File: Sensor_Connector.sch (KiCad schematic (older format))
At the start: 7 parts, among them J3 JST-GH

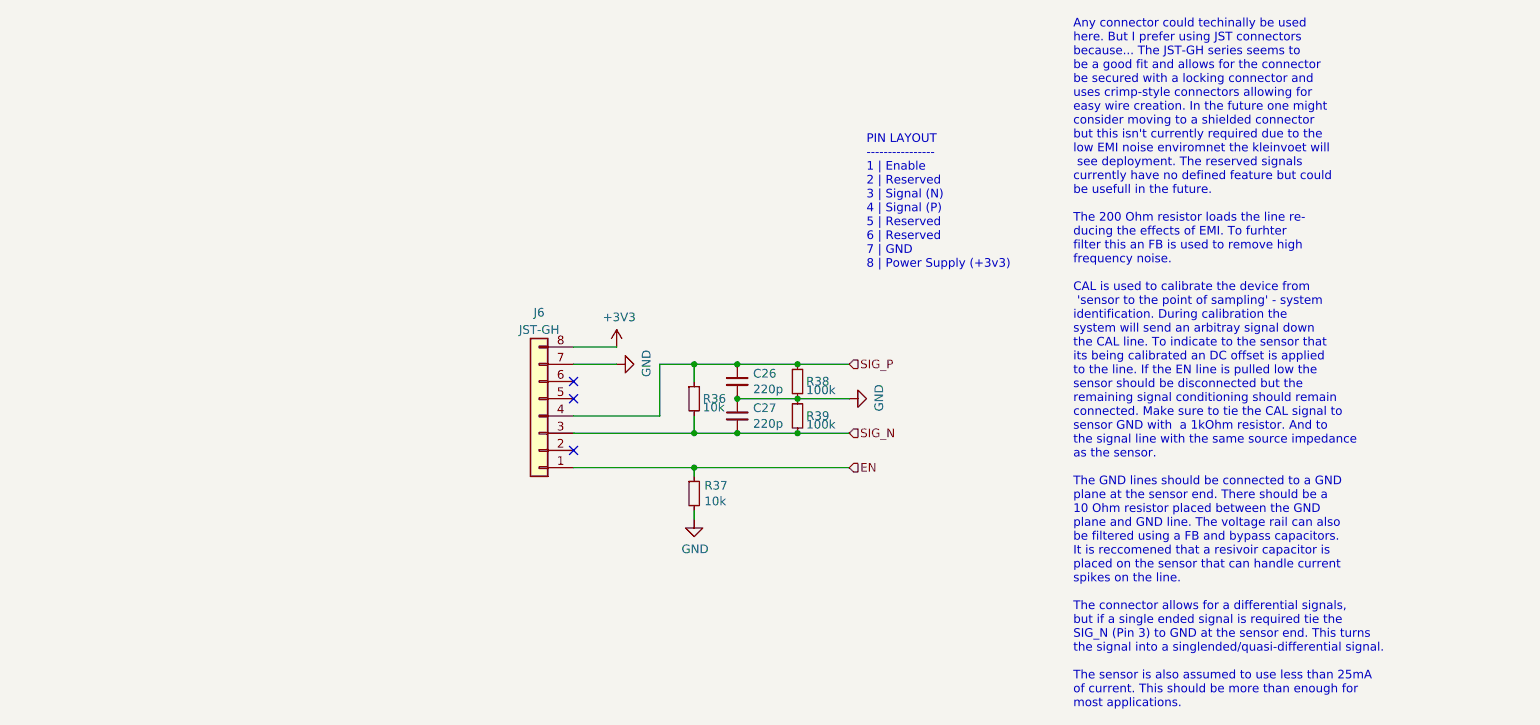
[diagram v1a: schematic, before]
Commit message: Change Mic Preamp
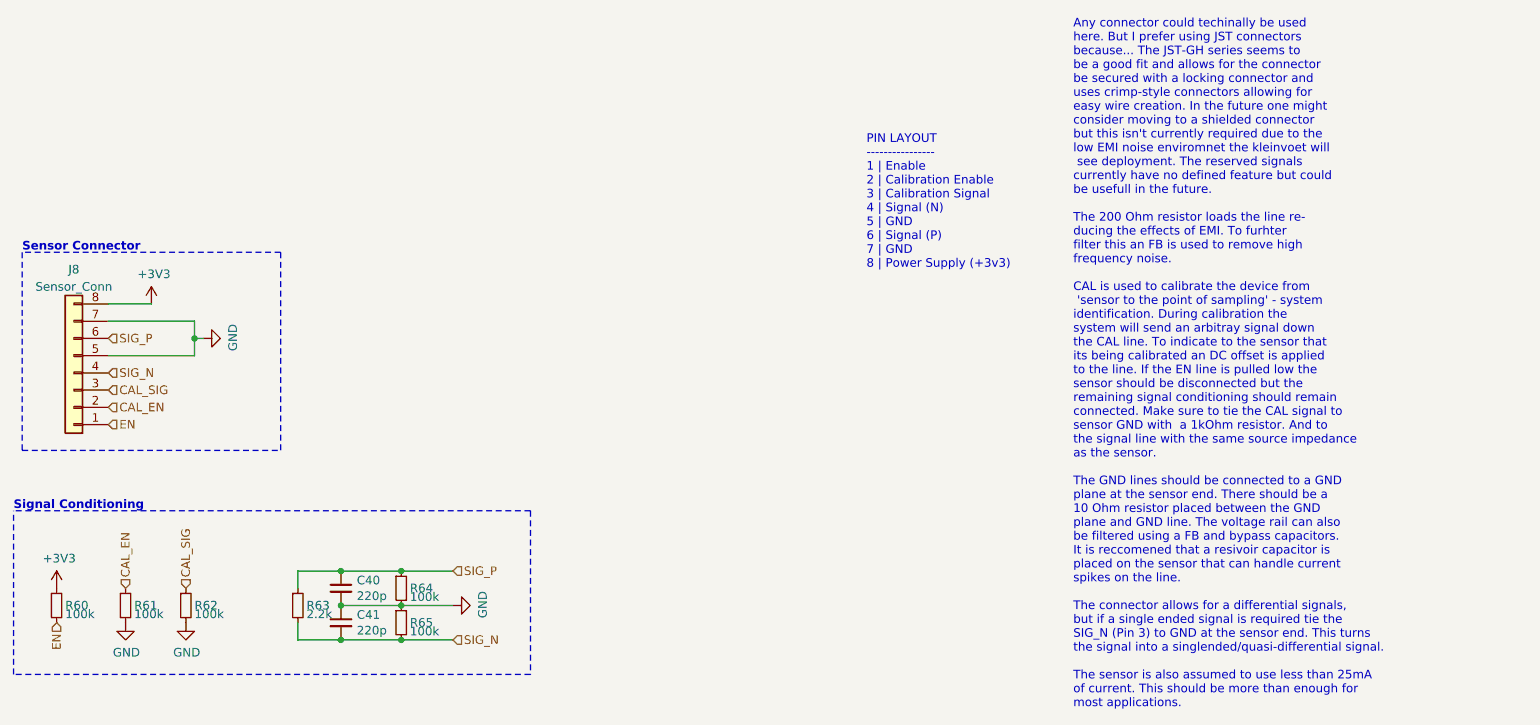
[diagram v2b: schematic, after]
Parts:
- added R24, R26: 100k, Resistor_SMD:R_0603_1608Metric_Pad1.05x0.95mm_HandSolder, symbol Device:R_Small
- J3: value JST-GH -> Sensor_Conn
- R25: value 10k -> 100k; MPN (none) -> RC0603FR-07100KL; Mfr. (none) -> Yageo
- R27: renamed from R24; value 10k -> 2.2k; MPN RC0603JR-0710KL -> RC0603FR-072K2L
- renumbered C20 to C18, C21 to C19, R26 to R28, R27 to R29
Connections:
- net +3V3: now also R24.1
- net EN: now also R24.2; no longer R25.1
- net GND: now also J3.5 (Pin_5), R26.2
- net SIG_N: now also J3.4 (Pin_4); no longer J3.3 (Pin_3)
- net SIG_P: now also J3.6 (Pin_6); no longer J3.4 (Pin_4)
- net CAL_EN: now reaches J3.2 (Pin_2)
- net CAL_EN: now also R25.1
- new net CAL_SIG: J3.3 (Pin_3), R26.1
- no-connect marks 3 -> 0
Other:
- note added: "PIN LAYOUT\n----------------\n1 | Enable\n2 | Calibration Enable\n3 | Calibration Signal\n4 | Signal (N)\n5 | GND\n6 | Signal (P)\n7 | GND\n8 | Power Supply (+3v3)"
- note added: "Sensor Connector"
- note added: "Signal Conditioning"
- note removed: "PIN LAYOUT\n----------------\n1 | Enable\n2 | Reserved\n3 | Signal (N)\n4 | Signal (P)\n5 | Reserved\n6 | Reserved\n7 | GND\n8 | Power Supply (+3v3)"
- moved on the sheet: C40, C41, J8, R63, R64, R65

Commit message: Fix BOM ref
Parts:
- C18, C19: MPN (none) -> C0603C221J5GACTU; Mfr. (none) -> KEMET
- J3: MPN (none) -> 53047-0810; Mfr. (none) -> Molex
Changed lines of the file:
@@
 $Descr A4 11693 8268
 encoding utf-8
-Sheet 12 15
+Sheet 7 17
 Title "Kleinvoet"
 Date "2020-06-11"
@@
 AR Path="/5EE5ECAD/5EFF6D57/5F1EB8A3" Ref="R57"  Part="1"
 AR Path="/5EE5ECAD/5EFFC4F7/5F1EB8A3" Ref="R63"  Part="1"
-F 0 "R63" H 3000 5000 50  0000 L CNN
+F 0 "R27" H 3000 5000 50  0000 L CNN
 F 1 "2.2k" H 3000 4950 50  0000 L CNN
 F 2 "Resistor_SMD:R_0603_1608Metric_Pad1.05x0.95mm_HandSolder" H 2950 5000 50  0001 C CNN
@@
 AR Path="/5EE5ECAD/5EFF6D57/5EEA2252" Ref="C38"  Part="1"
 AR Path="/5EE5ECAD/5EFFC4F7/5EEA2252" Ref="C40"  Part="1"
-F 0 "C40" H 3292 4946 50  0000 L CNN
+F 0 "C18" H 3292 4946 50  0000 L CNN
 F 1 "220p" H 3292 4855 50  0000 L CNN
 F 2 "Capacitor_SMD:C_0603_1608Metric_Pad1.05x0.95mm_HandSolder" H 3200 4900 50  0001 C CNN
 F 3 "~" H 3200 4900 50  0001 C CNN
+F 4 "C0603C221J5GACTU" H 3200 4900 50  0001 C CNN "MPN"
+F 5 "KEMET" H 3200 4900 50  0001 C CNN "Mfr."
 	1    3200 4900
 	1    0    0    -1
@@
 AR Path="/5EE5ECAD/5EFF6D57/5EEA248A" Ref="C39"  Part="1"
 AR Path="/5EE5ECAD/5EFFC4F7/5EEA248A" Ref="C41"  Part="1"
-F 0 "C41" H 3292 5146 50  0000 L CNN
+F 0 "C19" H 3292 5146 50  0000 L CNN
 F 1 "220p" H 3292 5055 50  0000 L CNN
 F 2 "Capacitor_SMD:C_0603_1608Metric_Pad1.05x0.95mm_HandSolder" H 3200 5100 50  0001 C CNN
 F 3 "~" H 3200 5100 50  0001 C CNN
+F 4 "C0603C221J5GACTU" H 3200 5100 50  0001 C CNN "MPN"
+F 5 "KEMET" H 3200 5100 50  0001 C CNN "Mfr."
 	1    3200 5100
 	1    0    0    -1
@@
 AR Path="/5EE5ECAD/5EFF6D57/5EEA3BAA" Ref="R58"  Part="1"
 AR Path="/5EE5ECAD/5EFFC4F7/5EEA3BAA" Ref="R64"  Part="1"
-F 0 "R64" H 3600 4900 50  0000 L CNN
+F 0 "R28" H 3600 4900 50  0000 L CNN
 F 1 "100k" H 3600 4850 50  0000 L CNN
 F 2 "Resistor_SMD:R_0603_1608Metric_Pad1.05x0.95mm_HandSolder" H 3550 4900 50  0001 C CNN
@@
 AR Path="/5EE5ECAD/5EFF6D57/5EEA3E65" Ref="R59"  Part="1"
 AR Path="/5EE5ECAD/5EFFC4F7/5EEA3E65" Ref="R65"  Part="1"
-F 0 "R65" H 3600 5100 50  0000 L CNN
+F 0 "R29" H 3600 5100 50  0000 L CNN
 F 1 "100k" H 3600 5050 50  0000 L CNN
 F 2 "Resistor_SMD:R_0603_1608Metric_Pad1.05x0.95mm_HandSolder" H 3550 5100 50  0001 C CNN
@@
 AR Path="/5EE5ECAD/5EFF6D57/5EEA4A0A" Ref="#PWR074"  Part="1"
 AR Path="/5EE5ECAD/5EFFC4F7/5EEA4A0A" Ref="#PWR080"  Part="1"
-F 0 "#PWR080" H 3850 4750 50  0001 C CNN
+F 0 "#PWR062" H 3850 4750 50  0001 C CNN
 F 1 "GND" H 3855 4827 50  0000 C CNN
 F 2 "" H 3850 5000 50  0001 C CNN
@@
 AR Path="/5EE5ECAD/5EFF6D57/5EFE739C" Ref="#PWR073"  Part="1"
 AR Path="/5EE5ECAD/5EFFC4F7/5EFE739C" Ref="#PWR079"  Part="1"
-F 0 "#PWR079" H 2400 3200 50  0001 C CNN
+F 0 "#PWR061" H 2400 3200 50  0001 C CNN
 F 1 "GND" H 2405 3277 50  0000 C CNN
 F 2 "" H 2400 3450 50  0001 C CNN
@@
 AR Path="/5EE5ECAD/5EFF6D57/5EE5C6A5" Ref="#PWR071"  Part="1"
 AR Path="/5EE5ECAD/5EFFC4F7/5EE5C6A5" Ref="#PWR077"  Part="1"
-F 0 "#PWR077" H 2100 3100 50  0001 C CNN
+F 0 "#PWR059" H 2100 3100 50  0001 C CNN
 F 1 "+3V3" H 2115 3423 50  0000 C CNN
 F 2 "" H 2100 3250 50  0001 C CNN
@@
 AR Path="/5EE5ECAD/5EFF6D57/5EDAD860" Ref="J7"  Part="1"
 AR Path="/5EE5ECAD/5EFFC4F7/5EDAD860" Ref="J8"  Part="1"
-F 0 "J8" H 1650 3050 50  0000 C CNN
+F 0 "J3" H 1650 3050 50  0000 C CNN
 F 1 "Sensor_Conn" H 1650 3150 50  0000 C CNN
 F 2 "Connector_Molex:Molex_PicoBlade_53047-0810_1x08_P1.25mm_Vertical" H 1650 3650 50  0001 C CNN
 F 3 "~" H 1650 3650 50  0001 C CNN
+F 4 "53047-0810" H 1650 3650 50  0001 C CNN "MPN"
+F 5 "Molex" H 1650 3650 50  0001 C CNN "Mfr."
 	1    1650 3650
 	-1   0    0    1
@@
 AR Path="/5EE5ECAD/5EFF6D57/5EFD0A68" Ref="#PWR069"  Part="1"
 AR Path="/5EE5ECAD/5EFFC4F7/5EFD0A68" Ref="#PWR075"  Part="1"
-F 0 "#PWR075" H 1550 4750 50  0001 C CNN
+F 0 "#PWR057" H 1550 4750 50  0001 C CNN
 F 1 "+3V3" H 1565 5073 50  0000 C CNN
 F 2 "" H 1550 4900 50  0001 C CNN
@@
 AR Path="/5EE5ECAD/5EFF6D57/5EFD56F5" Ref="#PWR070"  Part="1"
 AR Path="/5EE5ECAD/5EFFC4F7/5EFD56F5" Ref="#PWR076"  Part="1"
-F 0 "#PWR076" H 1950 4850 50  0001 C CNN
+F 0 "#PWR058" H 1950 4850 50  0001 C CNN
 F 1 "GND" H 1955 4927 50  0000 C CNN
 F 2 "" H 1950 5100 50  0001 C CNN
@@
 AR Path="/5EE5ECAD/5EFF6D57/5EFDA9C9" Ref="#PWR072"  Part="1"
 AR Path="/5EE5ECAD/5EFFC4F7/5EFDA9C9" Ref="#PWR078"  Part="1"
-F 0 "#PWR078" H 2300 4850 50  0001 C CNN
+F 0 "#PWR060" H 2300 4850 50  0001 C CNN
 F 1 "GND" H 2305 4927 50  0000 C CNN
 F 2 "" H 2300 5100 50  0001 C CNN
@@
 AR Path="/5EE5ECAD/5EFF6D57/5F0BA11A" Ref="R56"  Part="1"
 AR Path="/5EE5ECAD/5EFFC4F7/5F0BA11A" Ref="R62"  Part="1"
-F 0 "R62" H 2350 5000 50  0000 L CNN
+F 0 "R26" H 2350 5000 50  0000 L CNN
 F 1 "100k" H 2350 4950 50  0000 L CNN
 F 2 "Resistor_SMD:R_0603_1608Metric_Pad1.05x0.95mm_HandSolder" H 2300 5000 50  0001 C CNN
@@
 AR Path="/5EE5ECAD/5EFF6D57/5F0BB1FA" Ref="R55"  Part="1"
 AR Path="/5EE5ECAD/5EFFC4F7/5F0BB1FA" Ref="R61"  Part="1"
-F 0 "R61" H 2000 5000 50  0000 L CNN
+F 0 "R25" H 2000 5000 50  0000 L CNN
 F 1 "100k" H 2000 4950 50  0000 L CNN
 F 2 "Resistor_SMD:R_0603_1608Metric_Pad1.05x0.95mm_HandSolder" H 1950 5000 50  0001 C CNN
@@
 AR Path="/5EE5ECAD/5EFF6D57/5F0BB553" Ref="R54"  Part="1"
 AR Path="/5EE5ECAD/5EFFC4F7/5F0BB553" Ref="R60"  Part="1"
-F 0 "R60" H 1600 5000 50  0000 L CNN
+F 0 "R24" H 1600 5000 50  0000 L CNN
 F 1 "100k" H 1600 4950 50  0000 L CNN
 F 2 "Resistor_SMD:R_0603_1608Metric_Pad1.05x0.95mm_HandSolder" H 1550 5000 50  0001 C CNN

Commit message: Change Sensor Connectors
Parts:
- J3: footprint Connector_Molex:Molex_PicoBlade_53047-0810_1x08_P1.25mm_Vertical -> Connector_PinHeader_2.54mm:PinHeader_1x08_P2.54mm_Vertical; MPN 53047-0810 -> (none); Mfr. Molex -> (none)
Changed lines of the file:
@@
 $Descr A4 11693 8268
 encoding utf-8
-Sheet 7 17
+Sheet 11 17
 Title "Kleinvoet"
 Date "2020-06-11"
@@
 AR Path="/5EE5ECAD/5EFF6D57/5F1EB8A3" Ref="R57"  Part="1"
 AR Path="/5EE5ECAD/5EFFC4F7/5F1EB8A3" Ref="R63"  Part="1"
-F 0 "R27" H 3000 5000 50  0000 L CNN
+F 0 "R63" H 3000 5000 50  0000 L CNN
 F 1 "2.2k" H 3000 4950 50  0000 L CNN
 F 2 "Resistor_SMD:R_0603_1608Metric_Pad1.05x0.95mm_HandSolder" H 2950 5000 50  0001 C CNN
@@
 AR Path="/5EE5ECAD/5EFF6D57/5EEA2252" Ref="C38"  Part="1"
 AR Path="/5EE5ECAD/5EFFC4F7/5EEA2252" Ref="C40"  Part="1"
-F 0 "C18" H 3292 4946 50  0000 L CNN
+F 0 "C40" H 3292 4946 50  0000 L CNN
 F 1 "220p" H 3292 4855 50  0000 L CNN
 F 2 "Capacitor_SMD:C_0603_1608Metric_Pad1.05x0.95mm_HandSolder" H 3200 4900 50  0001 C CNN
@@
 AR Path="/5EE5ECAD/5EFF6D57/5EEA248A" Ref="C39"  Part="1"
 AR Path="/5EE5ECAD/5EFFC4F7/5EEA248A" Ref="C41"  Part="1"
-F 0 "C19" H 3292 5146 50  0000 L CNN
+F 0 "C41" H 3292 5146 50  0000 L CNN
 F 1 "220p" H 3292 5055 50  0000 L CNN
 F 2 "Capacitor_SMD:C_0603_1608Metric_Pad1.05x0.95mm_HandSolder" H 3200 5100 50  0001 C CNN
@@
 AR Path="/5EE5ECAD/5EFF6D57/5EEA3BAA" Ref="R58"  Part="1"
 AR Path="/5EE5ECAD/5EFFC4F7/5EEA3BAA" Ref="R64"  Part="1"
-F 0 "R28" H 3600 4900 50  0000 L CNN
+F 0 "R64" H 3600 4900 50  0000 L CNN
 F 1 "100k" H 3600 4850 50  0000 L CNN
 F 2 "Resistor_SMD:R_0603_1608Metric_Pad1.05x0.95mm_HandSolder" H 3550 4900 50  0001 C CNN
@@
 AR Path="/5EE5ECAD/5EFF6D57/5EEA3E65" Ref="R59"  Part="1"
 AR Path="/5EE5ECAD/5EFFC4F7/5EEA3E65" Ref="R65"  Part="1"
-F 0 "R29" H 3600 5100 50  0000 L CNN
+F 0 "R65" H 3600 5100 50  0000 L CNN
 F 1 "100k" H 3600 5050 50  0000 L CNN
 F 2 "Resistor_SMD:R_0603_1608Metric_Pad1.05x0.95mm_HandSolder" H 3550 5100 50  0001 C CNN
@@
 AR Path="/5EE5ECAD/5EFF6D57/5EEA4A0A" Ref="#PWR074"  Part="1"
 AR Path="/5EE5ECAD/5EFFC4F7/5EEA4A0A" Ref="#PWR080"  Part="1"
-F 0 "#PWR062" H 3850 4750 50  0001 C CNN
+F 0 "#PWR080" H 3850 4750 50  0001 C CNN
 F 1 "GND" H 3855 4827 50  0000 C CNN
 F 2 "" H 3850 5000 50  0001 C CNN
@@
 AR Path="/5EE5ECAD/5EFF6D57/5EFE739C" Ref="#PWR073"  Part="1"
 AR Path="/5EE5ECAD/5EFFC4F7/5EFE739C" Ref="#PWR079"  Part="1"
-F 0 "#PWR061" H 2400 3200 50  0001 C CNN
+F 0 "#PWR079" H 2400 3200 50  0001 C CNN
 F 1 "GND" H 2405 3277 50  0000 C CNN
 F 2 "" H 2400 3450 50  0001 C CNN
@@
 AR Path="/5EE5ECAD/5EFF6D57/5EE5C6A5" Ref="#PWR071"  Part="1"
 AR Path="/5EE5ECAD/5EFFC4F7/5EE5C6A5" Ref="#PWR077"  Part="1"
-F 0 "#PWR059" H 2100 3100 50  0001 C CNN
+F 0 "#PWR077" H 2100 3100 50  0001 C CNN
 F 1 "+3V3" H 2115 3423 50  0000 C CNN
 F 2 "" H 2100 3250 50  0001 C CNN
@@
 AR Path="/5EE5ECAD/5EFF6D57/5EDAD860" Ref="J7"  Part="1"
 AR Path="/5EE5ECAD/5EFFC4F7/5EDAD860" Ref="J8"  Part="1"
-F 0 "J3" H 1650 3050 50  0000 C CNN
+F 0 "J8" H 1650 3050 50  0000 C CNN
 F 1 "Sensor_Conn" H 1650 3150 50  0000 C CNN
-F 2 "Connector_Molex:Molex_PicoBlade_53047-0810_1x08_P1.25mm_Vertical" H 1650 3650 50  0001 C CNN
+F 2 "Connector_PinHeader_2.54mm:PinHeader_1x08_P2.54mm_Vertical" H 1650 3650 50  0001 C CNN
 F 3 "~" H 1650 3650 50  0001 C CNN
-F 4 "53047-0810" H 1650 3650 50  0001 C CNN "MPN"
-F 5 "Molex" H 1650 3650 50  0001 C CNN "Mfr."
+F 4 "" H 1650 3650 50  0001 C CNN "MPN"
+F 5 "" H 1650 3650 50  0001 C CNN "Mfr."
 	1    1650 3650
 	-1   0    0    1
@@
 AR Path="/5EE5ECAD/5EFF6D57/5EFD0A68" Ref="#PWR069"  Part="1"
 AR Path="/5EE5ECAD/5EFFC4F7/5EFD0A68" Ref="#PWR075"  Part="1"
-F 0 "#PWR057" H 1550 4750 50  0001 C CNN
+F 0 "#PWR075" H 1550 4750 50  0001 C CNN
 F 1 "+3V3" H 1565 5073 50  0000 C CNN
 F 2 "" H 1550 4900 50  0001 C CNN
@@
 AR Path="/5EE5ECAD/5EFF6D57/5EFD56F5" Ref="#PWR070"  Part="1"
 AR Path="/5EE5ECAD/5EFFC4F7/5EFD56F5" Ref="#PWR076"  Part="1"
-F 0 "#PWR058" H 1950 4850 50  0001 C CNN
+F 0 "#PWR076" H 1950 4850 50  0001 C CNN
 F 1 "GND" H 1955 4927 50  0000 C CNN
 F 2 "" H 1950 5100 50  0001 C CNN
@@
 AR Path="/5EE5ECAD/5EFF6D57/5EFDA9C9" Ref="#PWR072"  Part="1"
 AR Path="/5EE5ECAD/5EFFC4F7/5EFDA9C9" Ref="#PWR078"  Part="1"
-F 0 "#PWR060" H 2300 4850 50  0001 C CNN
+F 0 "#PWR078" H 2300 4850 50  0001 C CNN
 F 1 "GND" H 2305 4927 50  0000 C CNN
 F 2 "" H 2300 5100 50  0001 C CNN
@@
 AR Path="/5EE5ECAD/5EFF6D57/5F0BA11A" Ref="R56"  Part="1"
 AR Path="/5EE5ECAD/5EFFC4F7/5F0BA11A" Ref="R62"  Part="1"
-F 0 "R26" H 2350 5000 50  0000 L CNN
+F 0 "R62" H 2350 5000 50  0000 L CNN
 F 1 "100k" H 2350 4950 50  0000 L CNN
 F 2 "Resistor_SMD:R_0603_1608Metric_Pad1.05x0.95mm_HandSolder" H 2300 5000 50  0001 C CNN
@@
 AR Path="/5EE5ECAD/5EFF6D57/5F0BB1FA" Ref="R55"  Part="1"
 AR Path="/5EE5ECAD/5EFFC4F7/5F0BB1FA" Ref="R61"  Part="1"
-F 0 "R25" H 2000 5000 50  0000 L CNN
+F 0 "R61" H 2000 5000 50  0000 L CNN
 F 1 "100k" H 2000 4950 50  0000 L CNN
 F 2 "Resistor_SMD:R_0603_1608Metric_Pad1.05x0.95mm_HandSolder" H 1950 5000 50  0001 C CNN
@@
 AR Path="/5EE5ECAD/5EFF6D57/5F0BB553" Ref="R54"  Part="1"
 AR Path="/5EE5ECAD/5EFFC4F7/5F0BB553" Ref="R60"  Part="1"
-F 0 "R24" H 1600 5000 50  0000 L CNN
+F 0 "R60" H 1600 5000 50  0000 L CNN
 F 1 "100k" H 1600 4950 50  0000 L CNN
 F 2 "Resistor_SMD:R_0603_1608Metric_Pad1.05x0.95mm_HandSolder" H 1550 5000 50  0001 C CNN

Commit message: Setup PCB
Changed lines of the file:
@@
 $Descr A4 11693 8268
 encoding utf-8
-Sheet 11 17
+Sheet 7 17
 Title "Kleinvoet"
 Date "2020-06-11"
@@
 AR Path="/5EE5ECAD/5EFF6D57/5F1EB8A3" Ref="R57"  Part="1"
 AR Path="/5EE5ECAD/5EFFC4F7/5F1EB8A3" Ref="R63"  Part="1"
-F 0 "R63" H 3000 5000 50  0000 L CNN
+F 0 "R27" H 3000 5000 50  0000 L CNN
 F 1 "2.2k" H 3000 4950 50  0000 L CNN
 F 2 "Resistor_SMD:R_0603_1608Metric_Pad1.05x0.95mm_HandSolder" H 2950 5000 50  0001 C CNN
@@
 AR Path="/5EE5ECAD/5EFF6D57/5EEA2252" Ref="C38"  Part="1"
 AR Path="/5EE5ECAD/5EFFC4F7/5EEA2252" Ref="C40"  Part="1"
-F 0 "C40" H 3292 4946 50  0000 L CNN
+F 0 "C18" H 3292 4946 50  0000 L CNN
 F 1 "220p" H 3292 4855 50  0000 L CNN
 F 2 "Capacitor_SMD:C_0603_1608Metric_Pad1.05x0.95mm_HandSolder" H 3200 4900 50  0001 C CNN
@@
 AR Path="/5EE5ECAD/5EFF6D57/5EEA248A" Ref="C39"  Part="1"
 AR Path="/5EE5ECAD/5EFFC4F7/5EEA248A" Ref="C41"  Part="1"
-F 0 "C41" H 3292 5146 50  0000 L CNN
+F 0 "C19" H 3292 5146 50  0000 L CNN
 F 1 "220p" H 3292 5055 50  0000 L CNN
 F 2 "Capacitor_SMD:C_0603_1608Metric_Pad1.05x0.95mm_HandSolder" H 3200 5100 50  0001 C CNN
@@
 AR Path="/5EE5ECAD/5EFF6D57/5EEA3BAA" Ref="R58"  Part="1"
 AR Path="/5EE5ECAD/5EFFC4F7/5EEA3BAA" Ref="R64"  Part="1"
-F 0 "R64" H 3600 4900 50  0000 L CNN
+F 0 "R28" H 3600 4900 50  0000 L CNN
 F 1 "100k" H 3600 4850 50  0000 L CNN
 F 2 "Resistor_SMD:R_0603_1608Metric_Pad1.05x0.95mm_HandSolder" H 3550 4900 50  0001 C CNN
@@
 AR Path="/5EE5ECAD/5EFF6D57/5EEA3E65" Ref="R59"  Part="1"
 AR Path="/5EE5ECAD/5EFFC4F7/5EEA3E65" Ref="R65"  Part="1"
-F 0 "R65" H 3600 5100 50  0000 L CNN
+F 0 "R29" H 3600 5100 50  0000 L CNN
 F 1 "100k" H 3600 5050 50  0000 L CNN
 F 2 "Resistor_SMD:R_0603_1608Metric_Pad1.05x0.95mm_HandSolder" H 3550 5100 50  0001 C CNN
@@
 AR Path="/5EE5ECAD/5EFF6D57/5EEA4A0A" Ref="#PWR074"  Part="1"
 AR Path="/5EE5ECAD/5EFFC4F7/5EEA4A0A" Ref="#PWR080"  Part="1"
-F 0 "#PWR080" H 3850 4750 50  0001 C CNN
+F 0 "#PWR062" H 3850 4750 50  0001 C CNN
 F 1 "GND" H 3855 4827 50  0000 C CNN
 F 2 "" H 3850 5000 50  0001 C CNN
@@
 AR Path="/5EE5ECAD/5EFF6D57/5EFE739C" Ref="#PWR073"  Part="1"
 AR Path="/5EE5ECAD/5EFFC4F7/5EFE739C" Ref="#PWR079"  Part="1"
-F 0 "#PWR079" H 2400 3200 50  0001 C CNN
+F 0 "#PWR061" H 2400 3200 50  0001 C CNN
 F 1 "GND" H 2405 3277 50  0000 C CNN
 F 2 "" H 2400 3450 50  0001 C CNN
@@
 AR Path="/5EE5ECAD/5EFF6D57/5EE5C6A5" Ref="#PWR071"  Part="1"
 AR Path="/5EE5ECAD/5EFFC4F7/5EE5C6A5" Ref="#PWR077"  Part="1"
-F 0 "#PWR077" H 2100 3100 50  0001 C CNN
+F 0 "#PWR059" H 2100 3100 50  0001 C CNN
 F 1 "+3V3" H 2115 3423 50  0000 C CNN
 F 2 "" H 2100 3250 50  0001 C CNN
@@
 AR Path="/5EE5ECAD/5EFF6D57/5EDAD860" Ref="J7"  Part="1"
 AR Path="/5EE5ECAD/5EFFC4F7/5EDAD860" Ref="J8"  Part="1"
-F 0 "J8" H 1650 3050 50  0000 C CNN
+F 0 "J3" H 1650 3050 50  0000 C CNN
 F 1 "Sensor_Conn" H 1650 3150 50  0000 C CNN
 F 2 "Connector_PinHeader_2.54mm:PinHeader_1x08_P2.54mm_Vertical" H 1650 3650 50  0001 C CNN
@@
 AR Path="/5EE5ECAD/5EFF6D57/5EFD0A68" Ref="#PWR069"  Part="1"
 AR Path="/5EE5ECAD/5EFFC4F7/5EFD0A68" Ref="#PWR075"  Part="1"
-F 0 "#PWR075" H 1550 4750 50  0001 C CNN
+F 0 "#PWR057" H 1550 4750 50  0001 C CNN
 F 1 "+3V3" H 1565 5073 50  0000 C CNN
 F 2 "" H 1550 4900 50  0001 C CNN
@@
 AR Path="/5EE5ECAD/5EFF6D57/5EFD56F5" Ref="#PWR070"  Part="1"
 AR Path="/5EE5ECAD/5EFFC4F7/5EFD56F5" Ref="#PWR076"  Part="1"
-F 0 "#PWR076" H 1950 4850 50  0001 C CNN
+F 0 "#PWR058" H 1950 4850 50  0001 C CNN
 F 1 "GND" H 1955 4927 50  0000 C CNN
 F 2 "" H 1950 5100 50  0001 C CNN
@@
 AR Path="/5EE5ECAD/5EFF6D57/5EFDA9C9" Ref="#PWR072"  Part="1"
 AR Path="/5EE5ECAD/5EFFC4F7/5EFDA9C9" Ref="#PWR078"  Part="1"
-F 0 "#PWR078" H 2300 4850 50  0001 C CNN
+F 0 "#PWR060" H 2300 4850 50  0001 C CNN
 F 1 "GND" H 2305 4927 50  0000 C CNN
 F 2 "" H 2300 5100 50  0001 C CNN
@@
 AR Path="/5EE5ECAD/5EFF6D57/5F0BA11A" Ref="R56"  Part="1"
 AR Path="/5EE5ECAD/5EFFC4F7/5F0BA11A" Ref="R62"  Part="1"
-F 0 "R62" H 2350 5000 50  0000 L CNN
+F 0 "R26" H 2350 5000 50  0000 L CNN
 F 1 "100k" H 2350 4950 50  0000 L CNN
 F 2 "Resistor_SMD:R_0603_1608Metric_Pad1.05x0.95mm_HandSolder" H 2300 5000 50  0001 C CNN
@@
 AR Path="/5EE5ECAD/5EFF6D57/5F0BB1FA" Ref="R55"  Part="1"
 AR Path="/5EE5ECAD/5EFFC4F7/5F0BB1FA" Ref="R61"  Part="1"
-F 0 "R61" H 2000 5000 50  0000 L CNN
+F 0 "R25" H 2000 5000 50  0000 L CNN
 F 1 "100k" H 2000 4950 50  0000 L CNN
 F 2 "Resistor_SMD:R_0603_1608Metric_Pad1.05x0.95mm_HandSolder" H 1950 5000 50  0001 C CNN
@@
 AR Path="/5EE5ECAD/5EFF6D57/5F0BB553" Ref="R54"  Part="1"
 AR Path="/5EE5ECAD/5EFFC4F7/5F0BB553" Ref="R60"  Part="1"
-F 0 "R60" H 1600 5000 50  0000 L CNN
+F 0 "R24" H 1600 5000 50  0000 L CNN
 F 1 "100k" H 1600 4950 50  0000 L CNN
 F 2 "Resistor_SMD:R_0603_1608Metric_Pad1.05x0.95mm_HandSolder" H 1550 5000 50  0001 C CNN

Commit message: PCB Layout Checkpoint
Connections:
- net +3V3: now also J3.4 (Pin_4); no longer J3.8 (Pin_8)
- net CAL_EN: now also J3.6 (Pin_6); no longer J3.2 (Pin_2)
- net CAL_SIG: now also J3.7 (Pin_7); no longer J3.3 (Pin_3)
- net EN: now also J3.5 (Pin_5); no longer J3.1 (Pin_1)
- net GND: now also J3.3 (Pin_3), J3.8 (Pin_8); no longer J3.5 (Pin_5), J3.7 (Pin_7)
- net SIG_N: now also C18.1, J3.2 (Pin_2), R27.1, R28.1; no longer C19.2, J3.4 (Pin_4), R27.2, R29.2
- net SIG_P: now also C19.2, J3.1 (Pin_1), R27.2, R29.2; no longer C18.1, J3.6 (Pin_6), R27.1, R28.1
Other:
- moved on the sheet: C32, C33, R54, R55, R56

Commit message: Major Commit with Final PCB Design
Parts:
- removed R24, R25, R26: 100k, Resistor_SMD:R_0603_1608Metric_Pad1.05x0.95mm_HandSolder, symbol Device:R_Small
- J3: footprint Connector_PinHeader_2.54mm:PinHeader_1x08_P2.54mm_Vertical -> Connector_PinHeader_2.00mm:PinHeader_2x04_P2.00mm_Vertical; symbol Connector_Generic:Conn_01x08 -> Connector_Generic:Conn_02x04_Odd_Even
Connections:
- net +3V3: now also J3.1 (Pin_1); no longer J3.4 (Pin_4)
- net CAL_EN: now also J3.8 (Pin_8); no longer J3.6 (Pin_6)
- net EN: now also J3.6 (Pin_6); no longer J3.5 (Pin_5)
- net GND: now also J3.5 (Pin_5); no longer J3.8 (Pin_8)
- net SIG_N: now also J3.4 (Pin_4); no longer J3.2 (Pin_2)
- net SIG_P: now also J3.2 (Pin_2); no longer J3.1 (Pin_1)
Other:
- moved on the sheet: J7
